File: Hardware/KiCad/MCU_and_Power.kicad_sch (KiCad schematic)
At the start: 34 parts

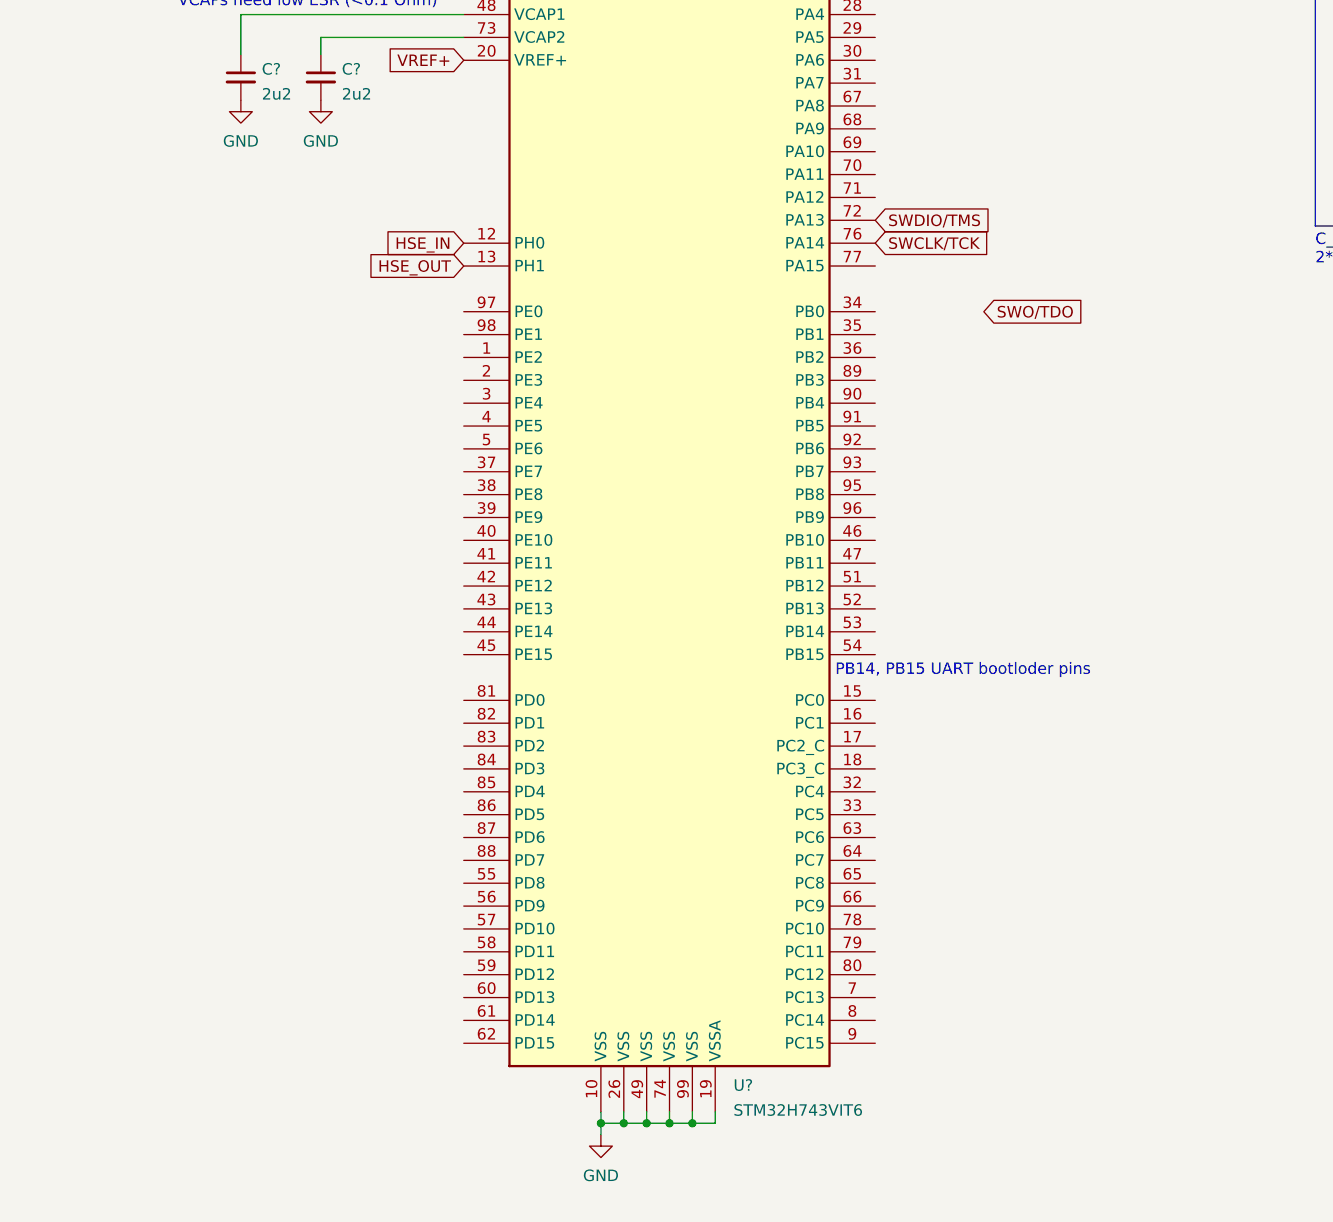
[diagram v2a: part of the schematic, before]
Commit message: Added some pin definitions and drivers for mcu communication
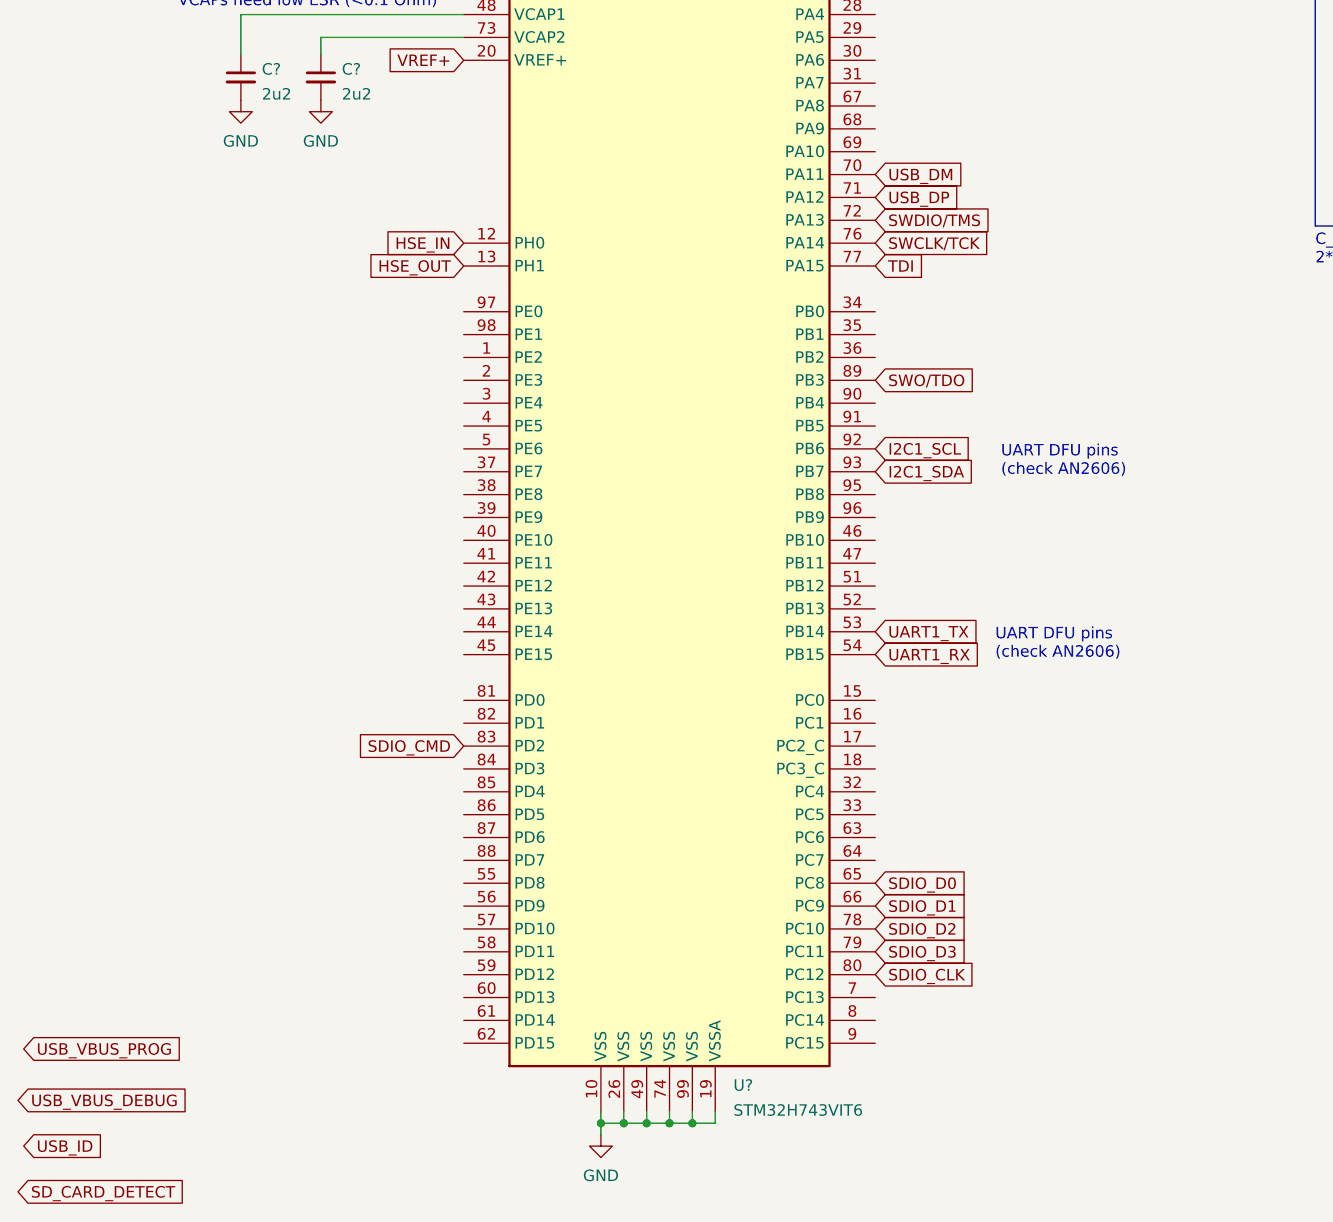
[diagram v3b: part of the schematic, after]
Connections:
- net SWO/TDO: now also U?.89 (PB3)
- net UART1_TX: now reaches U?.53 (PB14)
- net UART1_RX: now reaches U?.54 (PB15)
- net SDIO_D0: now reaches U?.65 (PC8)
- net SDIO_D1: now reaches U?.66 (PC9)
- net USB_DM: now reaches U?.70 (PA11)
- net USB_DP: now reaches U?.71 (PA12)
- net TDI: now reaches U?.77 (PA15)
- net SDIO_D2: now reaches U?.78 (PC10)
- net SDIO_D3: now reaches U?.79 (PC11)
- net SDIO_CLK: now reaches U?.80 (PC12)
- net SDIO_CMD: now reaches U?.83 (PD2)
- net I2C1_SCL: now reaches U?.92 (PB6)
- net I2C1_SDA: now reaches U?.93 (PB7)
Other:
- note added: "UART DFU pins (check AN2606)"
- note removed: "PB14, PB15 UART bootloder pins"
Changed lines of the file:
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@@
     (effects (font (size 2 2)) (justify left bottom))
   )
-  (text "PB14, PB15 UART bootloder pins" (at 105.41 131.445 0)
+  (text "UART DFU pins \n(check AN2606)" (at 123.19 129.54 0)
     (effects (font (size 1.27 1.27)) (justify left bottom))
   )
@@
     (effects (font (size 1.27 1.27)) (justify left bottom))
   )
+  (text "UART DFU pins \n(check AN2606)" (at 123.825 109.22 0)
+    (effects (font (size 1.27 1.27)) (justify left bottom))
+  )
   (text "Switch for DFU mode" (at 192.405 160.02 0)
     (effects (font (size 1.27 1.27)) (justify left bottom))
@@
     )
   )
+  (global_label "USB_ID" (shape input) (at 15.24 183.515 0) (fields_autoplaced)
+    (effects (font (size 1.27 1.27)) (justify left))
+    (property "Intersheet References" "${INTERSHEET_REFS}" (id 0) (at 24.3055 183.4356 0)
+      (effects (font (size 1.27 1.27)) (justify left) hide)
+    )
+  )
   (global_label "HSE_OUT" (shape input) (at 194.31 63.5 0) (fields_autoplaced)
     (effects (font (size 1.27 1.27)) (justify left))
@@
     )
   )
-  (global_label "SWO{slash}TDO" (shape input) (at 121.92 90.805 0) (fields_autoplaced)
-    (effects (font (size 1.27 1.27)) (justify left))
-    (property "Intersheet References" "${INTERSHEET_REFS}" (id 0) (at 133.2231 90.7256 0)
+  (global_label "I2C1_SDA" (shape input) (at 109.855 108.585 0) (fields_autoplaced)
+    (effects (font (size 1.27 1.27)) (justify left))
+    (property "Intersheet References" "${INTERSHEET_REFS}" (id 0) (at 121.0976 108.6644 0)
+      (effects (font (size 1.27 1.27)) (justify left) hide)
+    )
+  )
+  (global_label "SWO{slash}TDO" (shape input) (at 109.855 98.425 0) (fields_autoplaced)
+    (effects (font (size 1.27 1.27)) (justify left))
+    (property "Intersheet References" "${INTERSHEET_REFS}" (id 0) (at 121.1581 98.3456 0)
       (effects (font (size 1.27 1.27)) (justify left) hide)
     )
@@
     )
   )
+  (global_label "SDIO_CLK" (shape input) (at 109.855 164.465 0) (fields_autoplaced)
+    (effects (font (size 1.27 1.27)) (justify left))
+    (property "Intersheet References" "${INTERSHEET_REFS}" (id 0) (at 121.2186 164.3856 0)
+      (effects (font (size 1.27 1.27)) (justify left) hide)
+    )
+  )
+  (global_label "USB_VBUS_DEBUG" (shape input) (at 14.605 178.435 0) (fields_autoplaced)
+    (effects (font (size 1.27 1.27)) (justify left))
+    (property "Intersheet References" "${INTERSHEET_REFS}" (id 0) (at 33.9514 178.3556 0)
+      (effects (font (size 1.27 1.27)) (justify left) hide)
+    )
+  )
   (global_label "NRST" (shape input) (at 247.015 140.335 180) (fields_autoplaced)
     (effects (font (size 1.27 1.27)) (justify right))
@@
     )
   )
+  (global_label "SDIO_D3" (shape input) (at 109.855 161.925 0) (fields_autoplaced)
+    (effects (font (size 1.27 1.27)) (justify left))
+    (property "Intersheet References" "${INTERSHEET_REFS}" (id 0) (at 120.13 161.8456 0)
+      (effects (font (size 1.27 1.27)) (justify left) hide)
+    )
+  )
+  (global_label "USB_DP" (shape input) (at 109.855 78.105 0) (fields_autoplaced)
+    (effects (font (size 1.27 1.27)) (justify left))
+    (property "Intersheet References" "${INTERSHEET_REFS}" (id 0) (at 119.5857 78.0256 0)
+      (effects (font (size 1.27 1.27)) (justify left) hide)
+    )
+  )
+  (global_label "UART1_TX" (shape input) (at 109.855 126.365 0) (fields_autoplaced)
+    (effects (font (size 1.27 1.27)) (justify left))
+    (property "Intersheet References" "${INTERSHEET_REFS}" (id 0) (at 121.2791 126.2856 0)
+      (effects (font (size 1.27 1.27)) (justify left) hide)
+    )
+  )
+  (global_label "TDI" (shape input) (at 109.855 85.725 0) (fields_autoplaced)
+    (effects (font (size 1.27 1.27)) (justify left))
+    (property "Intersheet References" "${INTERSHEET_REFS}" (id 0) (at 115.1105 85.6456 0)
+      (effects (font (size 1.27 1.27)) (justify left) hide)
+    )
+  )
   (global_label "HSE_OUT" (shape input) (at 64.135 85.725 180) (fields_autoplaced)
     (effects (font (size 1.27 1.27)) (justify right))
@@
     )
   )
+  (global_label "SDIO_CMD" (shape input) (at 64.135 139.065 180) (fields_autoplaced)
+    (effects (font (size 1.27 1.27)) (justify right))
+    (property "Intersheet References" "${INTERSHEET_REFS}" (id 0) (at 52.3481 139.1444 0)
+      (effects (font (size 1.27 1.27)) (justify right) hide)
+    )
+  )
   (global_label "HSE_IN" (shape input) (at 64.135 83.185 180) (fields_autoplaced)
     (effects (font (size 1.27 1.27)) (justify right))
@@
     )
   )
+  (global_label "USB_VBUS_PROG" (shape input) (at 15.24 172.72 0) (fields_autoplaced)
+    (effects (font (size 1.27 1.27)) (justify left))
+    (property "Intersheet References" "${INTERSHEET_REFS}" (id 0) (at 33.4374 172.6406 0)
+      (effects (font (size 1.27 1.27)) (justify left) hide)
+    )
+  )
   (global_label "VREF+" (shape input) (at 64.135 62.865 180) (fields_autoplaced)
     (effects (font (size 1.27 1.27)) (justify right))
@@
     )
   )
+  (global_label "UART1_RX" (shape input) (at 109.855 128.905 0) (fields_autoplaced)
+    (effects (font (size 1.27 1.27)) (justify left))
+    (property "Intersheet References" "${INTERSHEET_REFS}" (id 0) (at 121.5814 128.8256 0)
+      (effects (font (size 1.27 1.27)) (justify left) hide)
+    )
+  )
+  (global_label "SDIO_D0" (shape input) (at 109.855 154.305 0) (fields_autoplaced)
+    (effects (font (size 1.27 1.27)) (justify left))
+    (property "Intersheet References" "${INTERSHEET_REFS}" (id 0) (at 120.13 154.2256 0)
+      (effects (font (size 1.27 1.27)) (justify left) hide)
+    )
+  )
+  (global_label "I2C1_SCL" (shape input) (at 109.855 106.045 0) (fields_autoplaced)
+    (effects (font (size 1.27 1.27)) (justify left))
+    (property "Intersheet References" "${INTERSHEET_REFS}" (id 0) (at 121.0371 106.1244 0)
+      (effects (font (size 1.27 1.27)) (justify left) hide)
+    )
+  )
+  (global_label "SDIO_D2" (shape input) (at 109.855 159.385 0) (fields_autoplaced)
+    (effects (font (size 1.27 1.27)) (justify left))
+    (property "Intersheet References" "${INTERSHEET_REFS}" (id 0) (at 120.13 159.3056 0)
+      (effects (font (size 1.27 1.27)) (justify left) hide)
+    )
+  )
+  (global_label "SD_CARD_DETECT" (shape input) (at 14.605 188.595 0) (fields_autoplaced)
+    (effects (font (size 1.27 1.27)) (justify left))
+    (property "Intersheet References" "${INTERSHEET_REFS}" (id 0) (at 33.1048 188.5156 0)
+      (effects (font (size 1.27 1.27)) (justify left) hide)
+    )
+  )
+  (global_label "USB_DM" (shape input) (at 109.855 75.565 0) (fields_autoplaced)
+    (effects (font (size 1.27 1.27)) (justify left))
+    (property "Intersheet References" "${INTERSHEET_REFS}" (id 0) (at 119.7671 75.4856 0)
+      (effects (font (size 1.27 1.27)) (justify left) hide)
+    )
+  )
+  (global_label "SDIO_D1" (shape input) (at 109.855 156.845 0) (fields_autoplaced)
+    (effects (font (size 1.27 1.27)) (justify left))
+    (property "Intersheet References" "${INTERSHEET_REFS}" (id 0) (at 120.13 156.7656 0)
+      (effects (font (size 1.27 1.27)) (justify left) hide)
+    )
+  )

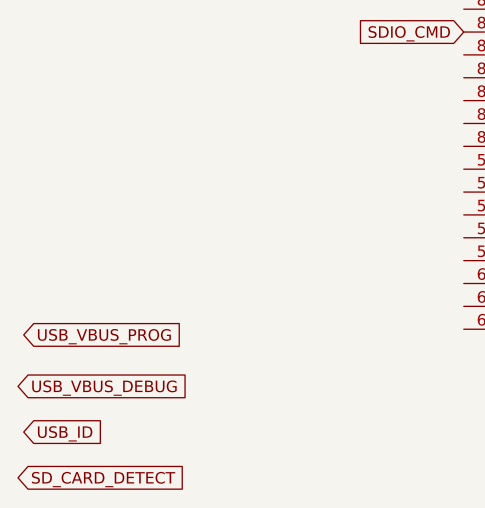
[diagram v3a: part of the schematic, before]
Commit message: Changed max PPM ESC controlers from 8->6 to make room for a buzzer and IBUS connection
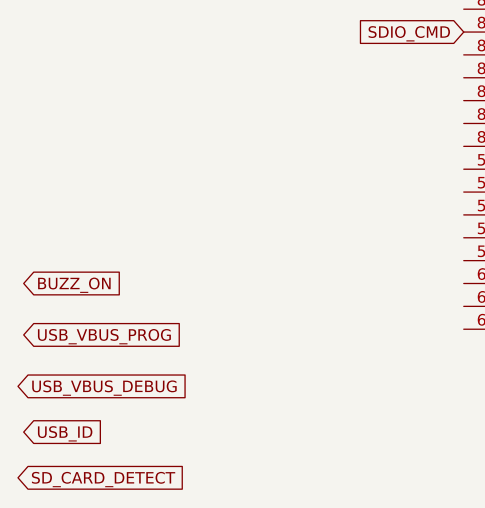
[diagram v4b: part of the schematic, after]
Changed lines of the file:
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@@
+    )
+  )
+  (global_label "BUZZ_ON" (shape input) (at 15.24 167.005 0) (fields_autoplaced)
+    (effects (font (size 1.27 1.27)) (justify left))
+    (property "Intersheet References" "${INTERSHEET_REFS}" (id 0) (at 26.3012 167.0844 0)
+      (effects (font (size 1.27 1.27)) (justify left) hide)
     )
   )
